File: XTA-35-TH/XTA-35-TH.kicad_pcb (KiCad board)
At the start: 4 copper layers, 222.1 x 98.7 mm, 27 parts, among them J1 XTA_Connector, U4 RPI_PICO

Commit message: Misc board work.
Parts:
- J3: renamed from XTA Power; value J3 -> XTA Power
- moved U4 146.9 mm to (177.2, 78.1), turned to 90 degrees
- moved C1 62.5 mm to (132.2, 57.7)
- moved C3 62.5 mm to (120.9, 57.7)
- moved R10 62.5 mm to (126.2, 61.0)
- moved R11 62.5 mm to (126.2, 64.3)
- moved C2 62.5 mm to (115.3, 57.7)
- moved D1 62.5 mm to (103.8, 57.7)
- moved D2 62.5 mm to (109.6, 57.7)
- moved R1 62.5 mm to (120.6, 64.3)
- moved R12 62.5 mm to (103.7, 67.6)
- moved R13 62.5 mm to (109.4, 67.6)
- moved R14 62.5 mm to (115.0, 67.6)
- moved R2 62.5 mm to (115.0, 64.3)
- moved R3 62.5 mm to (109.4, 64.3)
- moved R4 62.5 mm to (103.7, 64.3)
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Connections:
- J3 pad 1: (no net) -> Net-(J3-Pad1)
- J3 pad 2: (no net) -> GND
- J3 pad 3: (no net) -> GND
- J3 pad 4: (no net) -> IBM_5V_POWER
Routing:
- added copper zone on F.Cu, net (none)
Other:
- board size 222.1 x 98.7 mm -> 100 x 98.7 mm

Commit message: More board work.
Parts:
- removed D2: MBR120/130, Diode_SMD:D_SOD-123
- removed R12, R13, R14, R4, R5, R6: 10K, Resistor_SMD:R_1206_3216Metric
- added J4: LED, Connector_PinHeader_2.54mm:PinHeader_1x02_P2.54mm_Horizontal, F.Cu at (61.3, 65.0)
- added J5: Debug, Connector_PinHeader_2.54mm:PinHeader_1x06_P2.54mm_Vertical, F.Cu at (101.0, 64.1)
- added SW1: Config, 00Common:SW_DIP_SPSTx04, F.Cu at (92.0, 60.9)
- added SW2: Boot Internal, Button_Switch_THT:SW_PUSH_6mm, F.Cu at (108.0, 46.2)
- added SW3: Reset, Button_Switch_THT:SW_PUSH_6mm, F.Cu at (108.0, 37.6)
- added U1: 74LVC245, Package_DIP:DIP-20_W7.62mm_Socket, F.Cu at (72.8, 37.7)
- added U2: 74LVC245, Package_DIP:DIP-20_W7.62mm_Socket, F.Cu at (61.1, 37.7)
- added U3: 74HCT125, Package_DIP:DIP-14_W7.62mm_Socket, F.Cu at (96.3, 37.7)
- added U5: 74HC165, Package_DIP:DIP-16_W7.62mm_Socket, F.Cu at (84.6, 37.7)
- moved C3 47.6 mm to (75.2, 71.1)
- moved C2 41.3 mm to (75.2, 67.7)
- moved D1 29.3 mm to (75.3, 64.4)
- moved R3 22.6 mm to (119.4, 44.0)
- moved C4 21.6 mm to (119.4, 37.3)
- moved C1 21.3 mm to (119.4, 40.6)
- moved R2 17.6 mm to (119.4, 47.2)
- moved R10 16.1 mm to (110.5, 57.6)
- moved R11 16.1 mm to (110.5, 60.9)
- moved R9 14.0 mm to (116.1, 54.4)
- moved R1 13.8 mm to (119.4, 50.5)
- moved R7 8.01 mm to (110.5, 54.4)
- moved R8 3.43 mm to (110.5, 64.2)
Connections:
- R3 pad 1: IBM_SENSE_12V -> CFG_CLK
- R3 pad 2: Net-(R3-Pad2) -> CFG_DATA
- U4 pad 34: CFG_DATA -> SD1_CS
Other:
- outline, holes or cut-outs redrawn

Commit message: Lots of board layout.
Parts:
- added J2: SD0, 00Common:SD_Board, F.Cu at (181.6, 120.0)
- added J6: SD1, 00Common:SD_Board, F.Cu at (168.3, 100.3)
- added MH1: MountingHole_Pad, 00Common:Reinforcing_Ring_Partial, F.Cu at (164.4, 32.4)
- added MH2: MountingHole_Pad, 00Common:Reinforcing_Ring_Partial, F.Cu at (208.9, 32.4)
- added MH3: MountingHole_Pad, 00Common:Reinforcing_Ring_Partial, F.Cu at (164.4, 127.6)
- added MH4: MountingHole_Pad, 00Common:Reinforcing_Ring_Partial, F.Cu at (208.9, 127.6)
- added R4: 10K, Resistor_SMD:R_1206_3216Metric, F.Cu at (184.8, 37.5)
- moved D1 156.2 mm to (229.9, 41.9)
- moved U2 139.4 mm to (200.0, 48.9), turned to 90 degrees
- moved U4 135.2 mm to (198.1, 111.1), turned to 90 degrees
- moved R9 133.8 mm to (229.9, 121.3), turned to 90 degrees
- moved R8 132.5 mm to (226.7, 121.3), turned to 90 degrees
- moved R7 126.6 mm to (223.5, 121.3), turned to 90 degrees
- moved R5 126.0 mm to (217.2, 121.3), turned to 90 degrees
- moved SW1 124.8 mm to (204.5, 114.9), turned to 90 degrees
- moved C2 124.2 mm to (196.8, 42.5), turned to 270 degrees
- moved R6 123.8 mm to (220.3, 121.3), turned to 90 degrees
- moved U1 118.6 mm to (176.5, 95.2), turned to 90 degrees
- moved SW2 114.5 mm to (195.6, 120.0), turned to 180 degrees
- moved J5 106.7 mm to (207.6, 64.8)
- moved J4 102.7 mm to (161.3, 41.3), turned to 180 degrees
- moved C4 101.3 mm to (194.9, 104.8), turned to 270 degrees
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- renumbered R7 to R5, R8 to R6, R9 to R7, R10 to R8, R11 to R9, U5 to U4, U4 to U5
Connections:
- net IBM_5V_POWER renamed Net-(D1-Pad2)
- C3 pad 1: +3V3 -> VSYS
- C4 pad 1: VSYS -> +3V3
- J5 pad 2: Net-(J5-Pad2) -> GND
- J5 pad 5: Net-(J5-Pad2) -> GND
- R5 pad 1: Net-(R7-Pad1) -> Net-(R5-Pad1)
- R6 pad 1: Net-(R8-Pad1) -> Net-(R6-Pad1)
- R7 pad 1: Net-(R9-Pad1) -> Net-(R7-Pad1)
- R8 pad 1: Net-(R10-Pad1) -> Net-(R8-Pad1)
- SW1 pad 1: Net-(R7-Pad1) -> /RESET_INVERT
- SW1 pad 2: Net-(R8-Pad1) -> /IRQ_SELECT
- SW1 pad 3: Net-(R9-Pad1) -> /DRIVE_SIZE_2
- SW1 pad 4: Net-(R10-Pad1) -> /RESERVED
- SW1 pad 5: /RESERVED -> Net-(R8-Pad1)
- SW1 pad 6: /DRIVE_SIZE_2 -> Net-(R5-Pad1)
- SW1 pad 7: /IRQ_SELECT -> Net-(R6-Pad1)
- SW1 pad 8: /RESET_INVERT -> Net-(R7-Pad1)
- U3 pad 12: VSYS -> Net-(R4-Pad1)
- U3 pad 9: VSYS -> Net-(R4-Pad1)
- U4 pad 11: /RESET_INVERT -> /BOOT_INTERNAL
- U4 pad 12: /IRQ_SELECT -> GND
- U4 pad 13: /DRIVE_SIZE_2 -> GND
- U4 pad 14: /RESERVED -> GND
- U4 pad 3: /BOOT_INTERNAL -> /RESET_INVERT
- U4 pad 4: GND -> /IRQ_SELECT
- U4 pad 5: GND -> /DRIVE_SIZE_2
- U4 pad 6: GND -> /RESERVED
- U5 pad 10: D5_3V3 -> D1_3V3
- U5 pad 11: D6_3V3 -> D2_3V3
- U5 pad 12: D7_3V3 -> D3_3V3
- U5 pad 14: A0_3V3 -> D4_3V3
- U5 pad 15: A1_3V3 -> D5_3V3
- U5 pad 16: AEN_3V3 -> D6_3V3
- U5 pad 17: ~DACK~_3V3 -> D7_3V3
- U5 pad 19: ~DRQ~_3V3 -> A0_3V3
- U5 pad 20: ~IRQ~_3V3 -> A1_3V3
- U5 pad 34: SD1_CS -> CFG_LATCH
- U5 pad 4: D0_3V3 -> ~IRQ~_3V3
- U5 pad 42: Net-(J5-Pad2) -> GND
- U5 pad 5: D1_3V3 -> ~DRQ~_3V3
- U5 pad 6: D2_3V3 -> ~DACK~_3V3
- U5 pad 7: D3_3V3 -> AEN_3V3
- U5 pad 9: D4_3V3 -> D0_3V3
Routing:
- net +3V3: track 0.00 -> 217.6 mm, vias 0 -> 5
- net VSYS: track 0.00 -> 117.0 mm, vias 0 -> 6
- net D0: track 0.00 -> 64.1 mm
- net D1: track 0.00 -> 61.6 mm
- net D2: track 0.00 -> 59.0 mm
- net D3: track 0.00 -> 56.5 mm
- net D4: track 0.00 -> 53.4 mm
- net D5: track 0.00 -> 52.7 mm, vias 0 -> 1
- net D6: track 0.00 -> 52.7 mm, vias 0 -> 1
- net D7: track 0.00 -> 52.3 mm, vias 0 -> 1
- net /BOOT_INTERNAL: track 0.00 -> 39.7 mm, vias 0 -> 2
- net Net-(R1-Pad2): track 0.00 -> 26.6 mm, vias 0 -> 1
- net Net-(R7-Pad1): track 0.00 -> 22.6 mm, vias 0 -> 1
- net Net-(SW3-Pad1): track 0.00 -> 20.7 mm
- net Net-(R8-Pad1): track 0.00 -> 16.6 mm, vias 0 -> 1
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- added copper zone on F.Cu, net /MOUNTING_1
- added copper zone on F.Cu, net /MOUNTING_2
- added copper zone on F.Cu, net /MOUNTING_3
- added copper zone on B.Cu, net /MOUNTING_4
- added copper zone on F.Cu, net /MOUNTING_4
- added copper zone on In1.Cu, net /MOUNTING_4
- added copper zone on In2.Cu, net /MOUNTING_4
- removed copper zone on F.Cu, net (none)
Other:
- outline, holes or cut-outs redrawn

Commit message: Board layout WIP.
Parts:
- MH5, MH6, MH7, MH8: renamed from REF**; value MountingHole_3.2mm_M3_Pad -> MountingHole_Pad
- moved R3 10.2 mm to (212.1, 82.5), turned to 270 degrees
- moved SW2 8.28 mm to (188.6, 115.6), turned to 0 degrees
- moved J5 4.44 mm to (212.1, 64.8)
- moved R4 3.24 mm to (181.6, 38.1), turned to 0 degrees
- moved SW3 2.29 mm to (167.6, 51.4)
- moved R5 1.27 mm to (217.2, 122.6)
- moved R6 1.27 mm to (220.3, 122.6)
- moved R7 1.27 mm to (223.5, 122.6)
- moved R8 1.27 mm to (226.7, 122.6)
- moved R9 1.27 mm to (229.9, 122.6)
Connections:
- J2 pad 2: SD0_CS -> CFG_LATCH
- J6 pad 2: CFG_LATCH -> SD1_CS
- R3 pad 1: CFG_CLK -> DBG_RX
- U3 pad 10: ~DRQ~_3V3 -> CFG_CLK
- U3 pad 11: IRQ -> DRQ
- U3 pad 13: ~IRQ~_3V3 -> ~DRQ~_3V3
- U3 pad 3: ~DRIVE_ACTIVE -> Net-(R1-Pad2)
- U3 pad 4: CFG_CLK -> ~IRQ~_3V3
- U3 pad 5: GND -> Net-(R4-Pad1)
- U3 pad 6: Net-(R1-Pad2) -> IRQ
- U3 pad 8: DRQ -> ~DRIVE_ACTIVE
- U3 pad 9: Net-(R4-Pad1) -> GND
- U5 pad 22: SD0_CS -> ~CS~_3V3
- U5 pad 26: ~IOR~_3V3 -> ~IRQ~_3V3
- U5 pad 27: ~IOW~_3V3 -> ~DRQ~_3V3
- U5 pad 32: ~CS~_3V3 -> ~IOR~_3V3
- U5 pad 34: CFG_LATCH -> ~IOW~_3V3
- U5 pad 4: ~IRQ~_3V3 -> CFG_LATCH
- U5 pad 5: ~DRQ~_3V3 -> SD1_CS
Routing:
- net CFG_CLK: track 0.00 -> 146.8 mm, vias 0 -> 1
- net ~DRIVE_ACTIVE: track 0.00 -> 143.5 mm
- net DRQ: track 0.00 -> 109.8 mm, vias 0 -> 2
- net IRQ: track 0.00 -> 102.6 mm, vias 0 -> 2
- net A0: track 0.00 -> 91.4 mm, vias 0 -> 1
- net A1: track 0.00 -> 89.2 mm, vias 0 -> 1
- net ~CS: track 0.00 -> 88.9 mm, vias 0 -> 1
- net AEN: track 0.00 -> 74.9 mm, vias 0 -> 1
- net ~DACK: track 0.00 -> 72.6 mm, vias 0 -> 1
- net DBG_RX: track 0.00 -> 69.3 mm, vias 0 -> 1
- net ~IOR: track 0.00 -> 60.6 mm
- net SD_DO: track 0.00 -> 57.5 mm
- net ~IOW: track 0.00 -> 57.0 mm
- net +3V3: track 217.6 -> 273.6 mm, vias 5 -> 8
- net ~RESET~_3V3: track 0.00 -> 54.6 mm, vias 0 -> 1
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- added copper zone on B.Cu, net /MOUNTING_1
- added copper zone on In1.Cu, net /MOUNTING_1
- added copper zone on In2.Cu, net /MOUNTING_1
- added copper zone on B.Cu, net /MOUNTING_2
- added copper zone on In1.Cu, net /MOUNTING_2
- added copper zone on In2.Cu, net /MOUNTING_2
- added copper zone on B.Cu, net /MOUNTING_3
- added copper zone on In1.Cu, net /MOUNTING_3
- added copper zone on In2.Cu, net /MOUNTING_3

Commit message: Lots of board layout work.
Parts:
- moved SW2 17.3 mm to (205.7, 117.5)
- moved SW1 13.4 mm to (191.1, 116.2)
- moved R4 12.9 mm to (174.6, 48.9), turned to 180 degrees
- moved R8 10.2 mm to (227.3, 122.6), turned to 270 degrees
- moved R5 8.89 mm to (217.8, 122.6), turned to 270 degrees
- moved C4 8.26 mm to (186.7, 105.0)
- moved U4 8.25 mm to (189.9, 111.1)
- moved U3 3.81 mm to (175.3, 45.1)
- moved C3 3.61 mm to (172.1, 38.9)
- moved R3 1.91 mm to (214.0, 82.5)
- moved C1 0.76 mm to (174.0, 89.1)
- moved J5 0.63 mm to (212.7, 64.8)
- moved R6 0.63 mm to (221.0, 122.6), turned to 270 degrees
- moved R7 0.63 mm to (224.2, 122.6), turned to 270 degrees
- moved R9 0.63 mm to (230.5, 122.6), turned to 270 degrees
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- renumbered R8 to R5, R5 to R8
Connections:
- net Net-(D1-Pad2) renamed /5V_IN
- net Net-(U5-Pad35) renamed /ADC_VREF
- net Net-(U5-Pad37) renamed /3V3_EN
- R5 pad 1: Net-(R8-Pad1) -> +3V3
- R5 pad 2: +3V3 -> /IRQ_SELECT
- R6 pad 1: Net-(R6-Pad1) -> +3V3
- R6 pad 2: +3V3 -> /OPTION_3
- R7 pad 1: Net-(R7-Pad1) -> +3V3
- R7 pad 2: +3V3 -> /OPTION_4
- R8 pad 1: Net-(R5-Pad1) -> +3V3
- R8 pad 2: +3V3 -> /RESET_INVERT
- R9 pad 1: /BOOT_INTERNAL -> +3V3
- R9 pad 2: +3V3 -> /BOOT_INTERNAL
- SW1 pad 1: /RESET_INVERT -> /IRQ_SELECT
- SW1 pad 2: /IRQ_SELECT -> /RESET_INVERT
- SW1 pad 3: /DRIVE_SIZE_2 -> /OPTION_3
- SW1 pad 4: /RESERVED -> /OPTION_4
- SW1 pad 5: Net-(R8-Pad1) -> GND
- SW1 pad 6: Net-(R5-Pad1) -> GND
- SW1 pad 7: Net-(R6-Pad1) -> GND
- SW1 pad 8: Net-(R7-Pad1) -> GND
- U3 pad 1: CFG_CLK -> ~DRQ~_3V3
- U3 pad 11: DRQ -> Net-(R1-Pad2)
- U3 pad 12: Net-(R4-Pad1) -> GND
- U3 pad 13: ~DRQ~_3V3 -> CFG_CLK
- U3 pad 2: GND -> Net-(R4-Pad1)
- U3 pad 3: Net-(R1-Pad2) -> DRQ
- U4 pad 3: /RESET_INVERT -> /IRQ_SELECT
- U4 pad 4: /IRQ_SELECT -> /RESET_INVERT
- U4 pad 5: /DRIVE_SIZE_2 -> /OPTION_3
- U4 pad 6: /RESERVED -> /OPTION_4
- U5 pad 10: D1_3V3 -> D3_3V3
- U5 pad 11: D2_3V3 -> D4_3V3
- U5 pad 12: D3_3V3 -> D5_3V3
- U5 pad 14: D4_3V3 -> D6_3V3
- U5 pad 15: D5_3V3 -> D7_3V3
- U5 pad 16: D6_3V3 -> A0_3V3
- U5 pad 17: D7_3V3 -> A1_3V3
- U5 pad 19: A0_3V3 -> AEN_3V3
- U5 pad 20: A1_3V3 -> ~DACK~_3V3
- U5 pad 22: ~CS~_3V3 -> ~IOR~_3V3
- U5 pad 26: ~IRQ~_3V3 -> ~IOW~_3V3
- U5 pad 27: ~DRQ~_3V3 -> ~RESET~_3V3
- U5 pad 31: ~RESET~_3V3 -> ~CS~_3V3
- U5 pad 32: ~IOR~_3V3 -> ~IRQ~_3V3
- U5 pad 34: ~IOW~_3V3 -> ~DRQ~_3V3
- U5 pad 6: ~DACK~_3V3 -> D0_3V3
- U5 pad 7: AEN_3V3 -> D1_3V3
- U5 pad 9: D0_3V3 -> D2_3V3
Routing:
- net GND: track 0.27 -> 406.8 mm, vias 3 -> 52
- net DATA_DIR: track 0.00 -> 57.9 mm, vias 0 -> 2
- net CFG_LATCH: track 19.1 -> 74.4 mm, vias 0 -> 1
- net AEN_3V3: track 0.00 -> 44.1 mm
- net /RESET_INVERT: track 4.34 -> 47.7 mm, vias 0 -> 2
- net ~DACK~_3V3: track 0.00 -> 43.0 mm
- net SD_DI: track 46.7 -> 89.4 mm, vias 0 -> 1
- net SD_SCK: track 49.1 -> 89.7 mm, vias 0 -> 1
- net /OPTION_4: track 0.00 -> 37.7 mm, vias 0 -> 1
- net /IRQ_SELECT: track 4.34 -> 41.7 mm, vias 0 -> 2
- net SD_DO: track 57.5 -> 94.8 mm, vias 0 -> 1
- net /OPTION_3: track 0.00 -> 37.1 mm, vias 0 -> 1
- net Net-(R7-Pad1): track 23.1 -> 0.00 mm, vias 1 -> 0
- net ~DRQ~_3V3: track 0.00 -> 20.3 mm
- net /BOOT_INTERNAL: track 65.7 -> 45.7 mm, vias 3 -> 1
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- added copper zone on In1.Cu, net +3V3
- added copper zone on In2.Cu, net +3V3
- added copper zone on F.Cu, net /5V_IN
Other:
- board text added: "+"
- board text added: "+5V"
- board text added: "-"
- board text added: "1"
- board text added: "10Kx5"
- board text added: "120Rx2"
- board text added: "2"
- board text added: "3"
- board text added: "4"
- board text added: "LED"
- board text added: "OPTIONS"
- board text added: "PRIMARY SD CARD"
- board text added: "RESET"
- board text added: "SECONDARY SD CARD"
- board text added: "VIRTUAL FLOPPY BOOT"

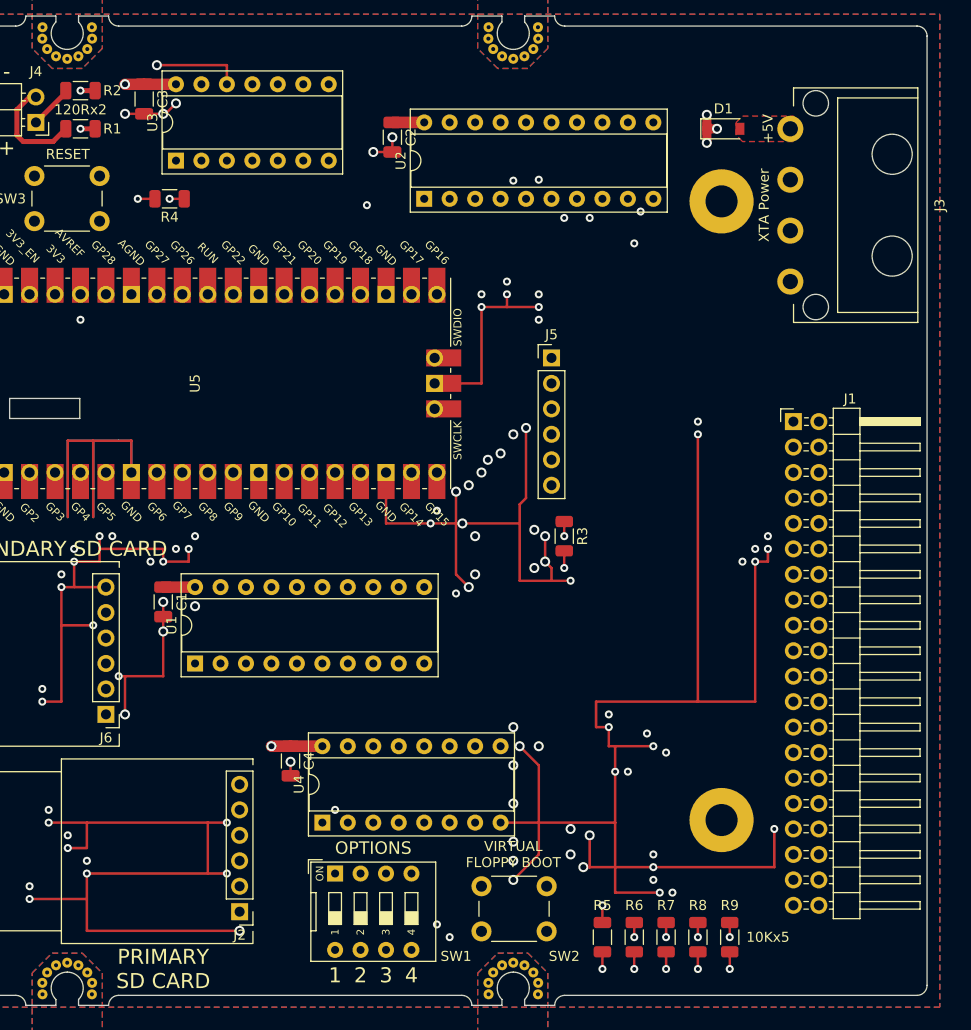
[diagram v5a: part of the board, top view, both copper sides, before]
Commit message: Finished first pass on copper layers.
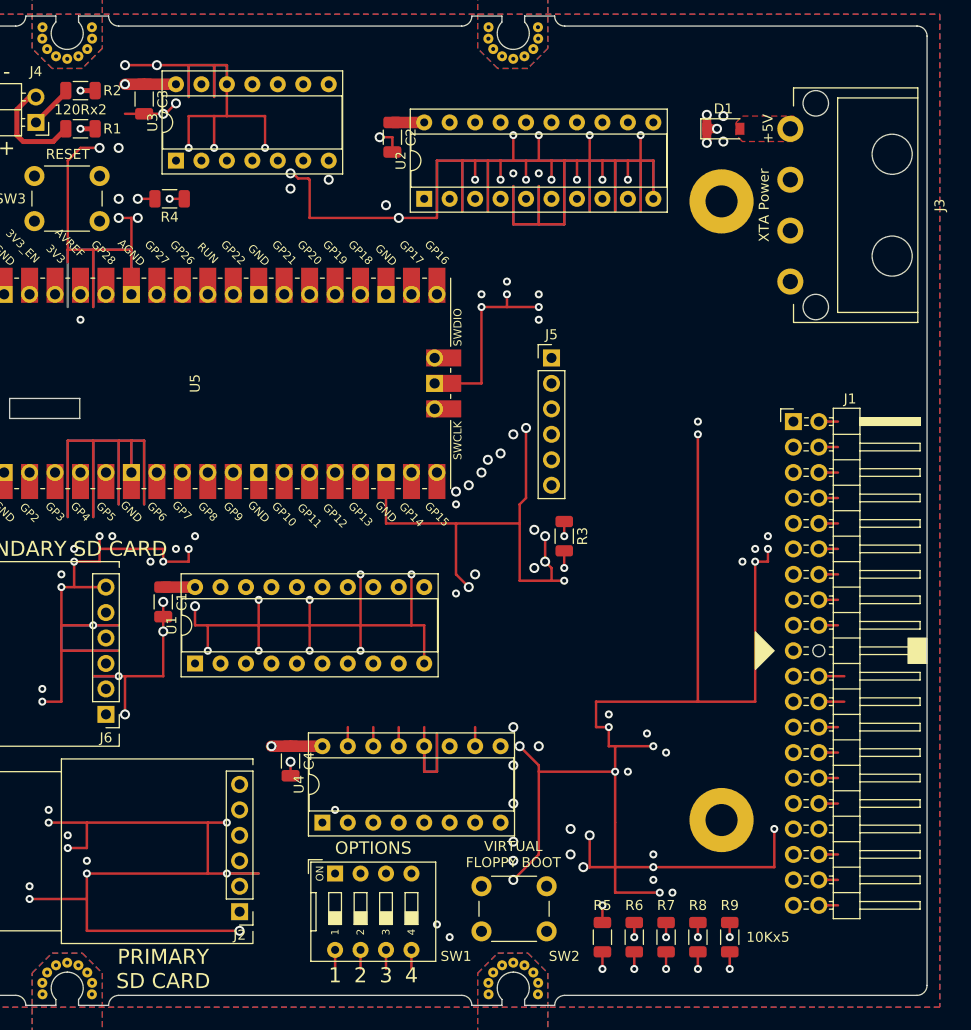
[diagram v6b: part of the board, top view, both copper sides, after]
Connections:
- U5 pad 22: ~IOR~_3V3 -> ~IOW~_3V3
- U5 pad 26: ~IOW~_3V3 -> ~IOR~_3V3
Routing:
- net GND: track 406.8 -> 874.3 mm, vias 52 -> 78
- net VSYS: track 117.8 -> 73.8 mm, vias 6 -> 8
- net ~IOW~_3V3: track 47.3 -> 37.2 mm, vias 1 -> 0
- net ~IOR~_3V3: track 37.7 -> 45.2 mm, vias 1 -> 0
- net +3V3: track 265.5 -> 258.3 mm, vias 23 -> 24
- net CFG_CLK: track 161.4 -> 163.8 mm
- net IRQ: track 103.3 -> 105.7 mm
- net AEN_3V3: track 44.1 -> 46.0 mm
- net ~DACK~_3V3: track 43.0 -> 44.9 mm
- net DRQ: track 109.6 -> 111.4 mm
- net D7_3V3: track 16.2 -> 17.7 mm
- net D6_3V3: track 16.2 -> 17.3 mm
- net D5_3V3: track 18.7 -> 19.8 mm
- net D5: track 52.6 -> 53.7 mm
- net D4: track 53.3 -> 54.4 mm
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- added copper zone on In1.Cu, net VSYS
- added copper zone on In2.Cu, net VSYS

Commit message: Finished first pass of board design.
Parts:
- J1: footprint Connector_PinHeader_2.54mm:PinHeader_2x20_P2.54mm_Horizontal -> Connector_IDC:IDC-Header_2x20_P2.54mm_Horizontal
- U5: value RPI_PICO -> Raspberry Pi Pico
- renumbered J3 to J2, J4 to J3, J2 to J4, J6 to J5, J5 to J6
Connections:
- net Net-(J5-Pad1) renamed /SWDIO
- net Net-(J5-Pad3) renamed /SWCLK
- net SD_SCK renamed SPI_SCK
- J4 pad 3: SD_DO -> SPI_TX
- J4 pad 5: SD_DI -> SPI_RX
- J5 pad 3: SD_DO -> SPI_TX
- J5 pad 5: SD_DI -> SPI_RX
- U5 pad 21: SD_DO -> SPI_RX
- U5 pad 25: SD_DI -> SPI_TX
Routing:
- net SPI_RX: track 0.00 -> 97.9 mm, vias 0 -> 2
- net SD_DO: track 94.8 -> 0.00 mm, vias 1 -> 0
- net SPI_TX: track 0.00 -> 91.2 mm, vias 0 -> 2
- net SD_DI: track 89.4 -> 0.00 mm, vias 1 -> 0
- net GND: track 874.3 -> 896.4 mm, vias 78 -> 80
- net VSYS: track 73.8 -> 63.5 mm, vias 8 -> 6
- net Net-(R4-Pad1): track 16.1 -> 13.3 mm
- net ~DRQ~_3V3: track 19.3 -> 17.0 mm
- net ~DRIVE_ACTIVE: track 141.8 -> 144.0 mm
- net CFG_CLK: track 163.8 -> 162.4 mm, vias 1 -> 2
- net DRQ: track 111.4 -> 112.2 mm
- removed copper zone on In2.Cu, net VSYS
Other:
- outline, holes or cut-outs redrawn
- board text added: "All capacitors and resistors are 1206 package."
- board text added: "Copyright (C) 2021 Titanium Studios Pty Ltd Creative Commons Attribution-ShareAlike 4.0 International https://github.com/ JayesonLS/8-bit-ide"
- board text added: "For systems with 8 bit IDE (XTA, XT-BUS) interfaces only. Never connect two drives to the same ribbon cable except in systems with special cross-wired cable."
- board text added: "IntelliDrive XTA-35"
- board text added: "MBR120 or MBR130 SOD-123"
- board text added: "OPTIONS: 1 IRQ selection. OFF: Default. ON: Alternate Requires mainboard / interface card IRQ to be set to match. 2. Reset level. OFF: Low, ON: High 3. Reserved for future use. 4. Reserved for future use."
- board text added: "See other side for options."
- board text added: "v0.1"
